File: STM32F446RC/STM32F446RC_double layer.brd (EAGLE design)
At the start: 80.2 x 26.9 mm, 75 parts, among them IC1 STM32F446RCT6

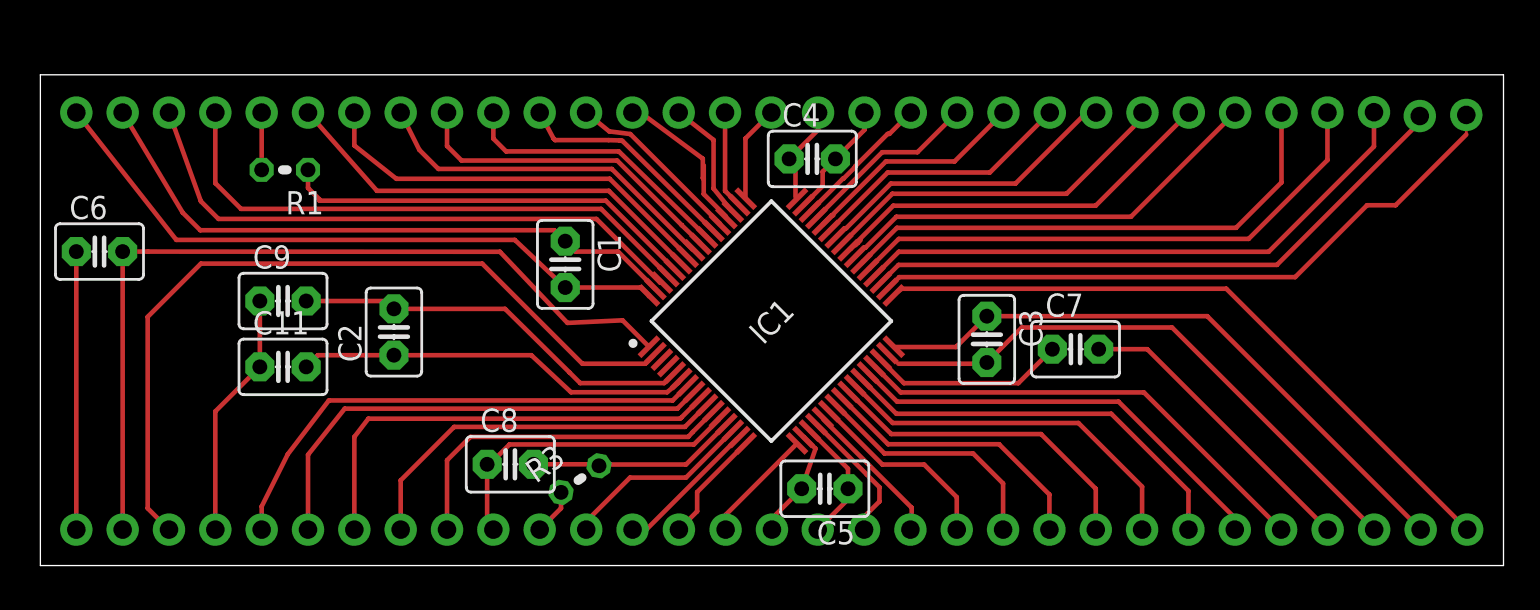
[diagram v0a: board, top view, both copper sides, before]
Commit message: added double layer
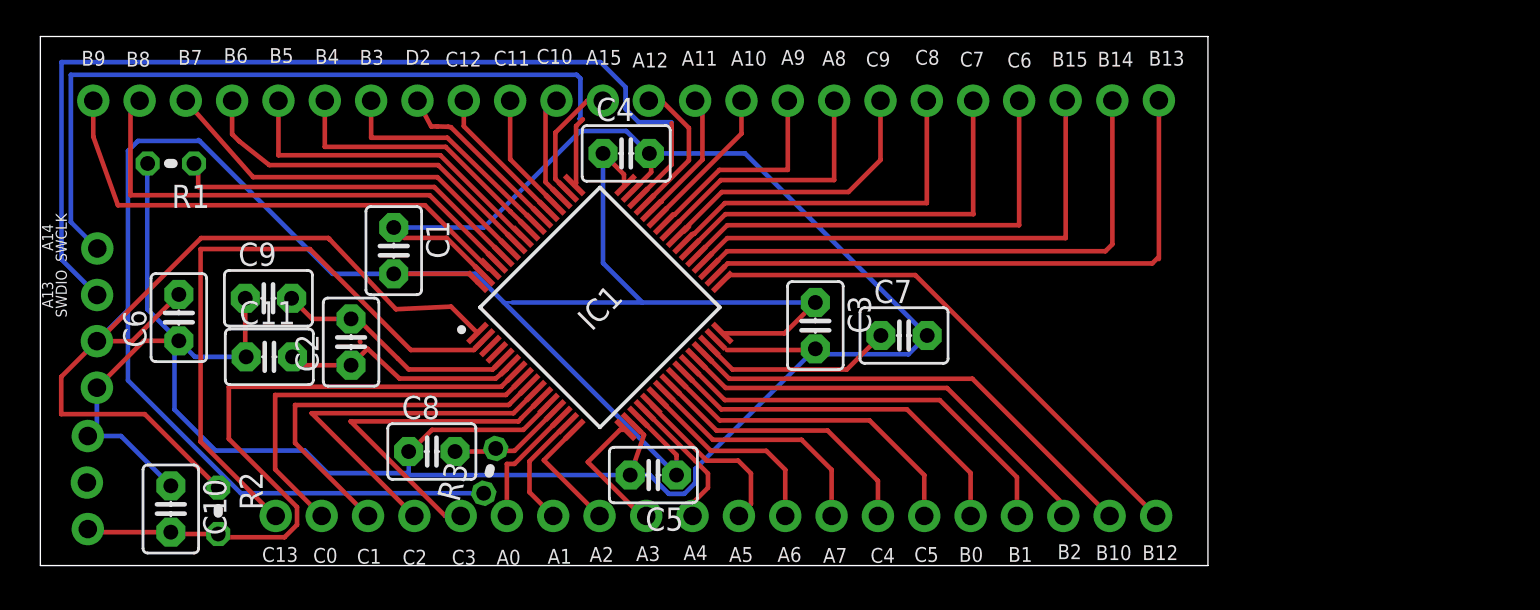
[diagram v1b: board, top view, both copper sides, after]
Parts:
- removed JP50, JP51, JP52, JP53, JP56, JP57, JP58, JP59, JP61, JP62, JP63, JP65: (no value), F405Pill:1X1-HEADER-HOLE
- added C10: 100n, capacitor-wima:C2.5-3
- added JP8: (no value), F405Pill:1X1-HEADER-HOLE
- added R2: 10k, rcl:0204V
- C1, C3, C4, C5, C6: value 100n+1u -> 100n
- R3: value (none) -> 47
- moved JP49 68.2 mm to (2.60, 7.10)
- moved JP54 45.7 mm to (3.11, 14.8)
- moved JP48 40.1 mm to (2.55, 4.55)
- moved JP55 37.7 mm to (3.12, 17.4)
- moved JP20 37.5 mm to (2.60, 2.00)
- moved JP18 17.1 mm to (61.2, 2.72)
- moved JP30 16.9 mm to (46.0, 25.5)
- moved JP1 16.9 mm to (53.6, 25.5)
- moved JP15 16.9 mm to (51.1, 25.5)
- moved JP25 16.9 mm to (33.4, 25.5)
- moved JP28 16.9 mm to (43.5, 25.5)
- moved JP31 16.9 mm to (41.0, 25.5)
- moved JP32 16.9 mm to (35.9, 25.5)
- moved JP33 16.9 mm to (38.4, 25.5)
- moved JP10 16.9 mm to (56.2, 25.5)
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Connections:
- removed net N$1: C3.2, IC1.31, JP50.1
- removed net N$4: C5.2, IC1.18, JP20.1
- removed net N$54: C7.2, JP49.1
- removed net N$55: C3.1, IC1.32, JP51.1
- removed net N$56: C4.2, IC1.47, JP52.1
- removed net N$57: JP56.1, R1.2
- removed net N$58: C6.2, IC1.1, JP7.1
- removed net N$59: C8.1, IC1.12, JP62.1
- removed net N$6: C1.2, IC1.64, JP58.1
- removed net N$60: JP61.1, R3.1
- removed net N$63: C11.1, C9.1, JP65.1
- removed net N$64: C5.1, IC1.19, JP48.1
- removed net N$67: C6.1, JP59.1
- removed net N$8: C1.1, IC1.63, JP57.1
- removed net N$89: C4.1, IC1.48, JP53.1
- new net GND: C1.1, C10.1, C11.1, C3.2, C4.2, C5.2, C6.1, C7.2, C8.1, C9.1, IC1.12, IC1.18, IC1.31, IC1.47, IC1.63, JP49.1, JP7.1, R1.2
- new net VDD: C1.2, C3.1, C4.1, C5.1, C6.2, IC1.1, IC1.19, IC1.32, IC1.48, IC1.64, JP8.1, R2.1, R3.1
- net N$3: now also C10.2, JP20.1, R2.2; no longer JP63.1
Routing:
- net VDD: track 0.00 -> 167.1 mm
- net GND: track 0.00 -> 147.2 mm
- net SWDIO: track 7.80 -> 54.8 mm
- net N$58: track 46.5 -> 0.00 mm
- net SWCLK: track 5.31 -> 44.3 mm
- net N$6: track 36.3 -> 0.00 mm
- net N$55: track 34.4 -> 0.00 mm
- net N$8: track 34.3 -> 0.00 mm
- net N$1: track 32.4 -> 0.00 mm
- net N$59: track 17.8 -> 0.00 mm
- net N$54: track 16.8 -> 0.00 mm
- net N$67: track 15.2 -> 0.00 mm
- net N$63: track 13.5 -> 0.00 mm
- net N$33: track 43.7 -> 34.4 mm
- net N$53: track 22.6 -> 13.6 mm
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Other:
- board size 80.2 x 26.9 mm -> 64 x 29 mm
- board text added: "A0"
- board text added: "A1"
- board text added: "A10"
- board text added: "A11"
- board text added: "A12"
- board text added: "A13"
- board text added: "A14"
- board text added: "A15"
- board text added: "A2"
- board text added: "A3"
- board text added: "A4"
- board text added: "A5"
- board text added: "A6"
- board text added: "A7"
- board text added: "A8"
- board text added: "A9"
- board text added: "B0"
- board text added: "B1"
- board text added: "B10"
- board text added: "B12"
- board text added: "B13"
- board text added: "B14"
- board text added: "B15"
- board text added: "B2"
- board text added: "B3"
- board text added: "B4"
- board text added: "B5"
- board text added: "B6"
- board text added: "B7"
- board text added: "B8"
- board text added: "B9"
- board text added: "C0"
- board text added: "C1"
- board text added: "C10"
- board text added: "C11"
- board text added: "C12"
- board text added: "C13"
- board text added: "C2"
- board text added: "C3"
- board text added: "C4"
- board text added: "C5"
- board text added: "C6"
- board text added: "C7"
- board text added: "C8"
- board text added: "C9"
- board text added: "D2"
- board text added: "SWCLK"
- board text added: "SWDIO"

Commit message: added double layer
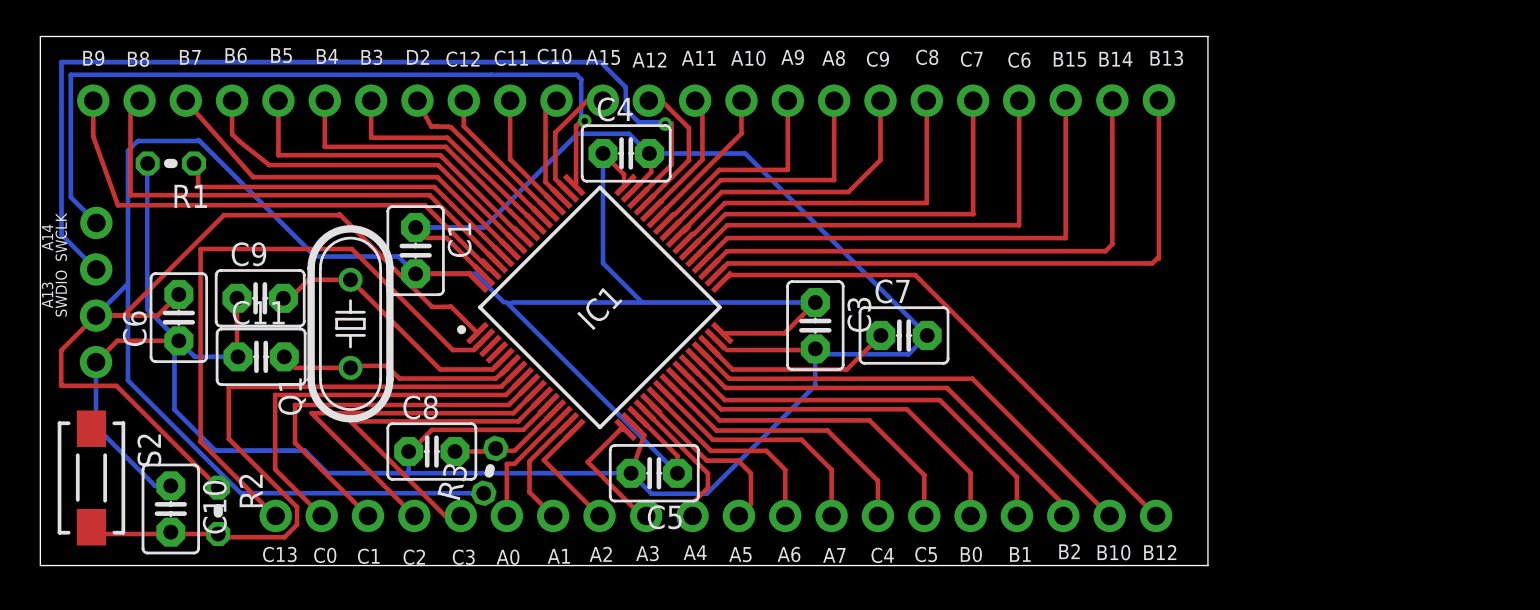
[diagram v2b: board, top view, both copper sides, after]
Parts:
- removed C2: 22p, capacitor-wima:C2.5-3
- removed JP20, JP48, JP49: (no value), F405Pill:1X1-HEADER-HOLE
- added Q1: (no value), crystal:HC49/S
- added S2: DTSM-3, switch-tact:DTSM-3
- moved JP55 1.40 mm to (3.07, 18.8)
- moved JP54 1.40 mm to (3.06, 16.2)
- moved JP7 1.40 mm to (3.05, 11.2)
- moved JP8 1.40 mm to (3.05, 13.7)
- moved C1 1.20 mm to (20.6, 17.3)
- moved C11 0.45 mm to (12.1, 11.4)
- moved C9 0.45 mm to (12.1, 14.7)
- moved C5 0.11 mm to (33.6, 5.06)
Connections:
- net GND: now also S2.1; no longer JP49.1
- net N$3: now also S2.2; no longer JP20.1
- net N$53: now also Q1.2; no longer C2.2
- net N$7: now also Q1.1; no longer C2.1
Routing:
- net VDD: track 167.1 -> 164.0 mm
- net SWDIO: track 54.8 -> 52.2 mm, vias 0 -> 1
- net GND: track 147.2 -> 145.3 mm
- net N$53: track 13.6 -> 14.9 mm
- net SWCLK: track 44.3 -> 43.0 mm, vias 0 -> 1
